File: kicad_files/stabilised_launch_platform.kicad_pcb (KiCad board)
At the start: 2 copper layers, 77 x 64.6 mm, 37 parts, among them J1 Conn_01x03_Male, J2 Conn_01x03_Male, J3 Conn_01x06_Male, J4 USB_C_Receptacle_USB2.0, SW1 SW_Push, U1 MAX7375AXR805, U2 AP7370-33Y, U3 STM32L011F3Px, U4 FT201XS, U5 LIS3DH

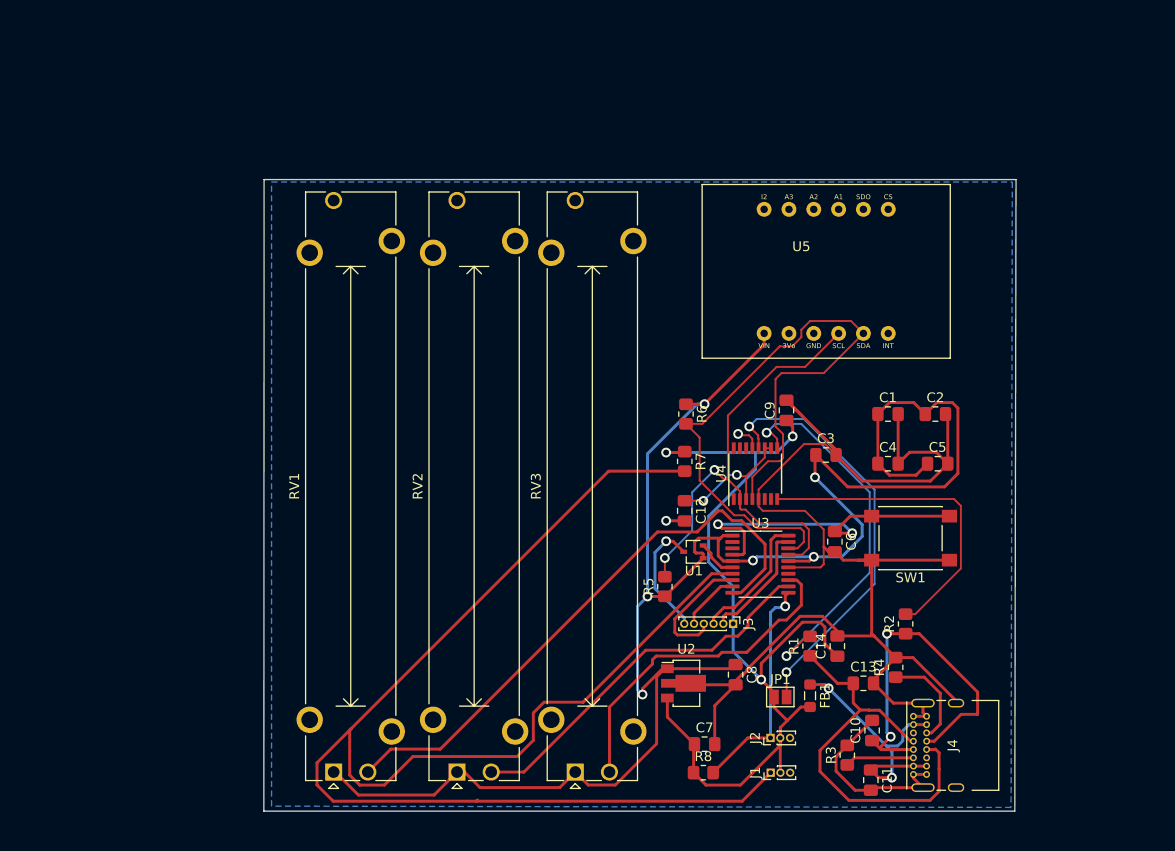
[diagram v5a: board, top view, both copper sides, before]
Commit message: PCB modifications: R1 and R2 moved closer to ftdi chip, 3.5mm diameter screw holes added, rounded PCB corners, C14 now electrolyic capacitor
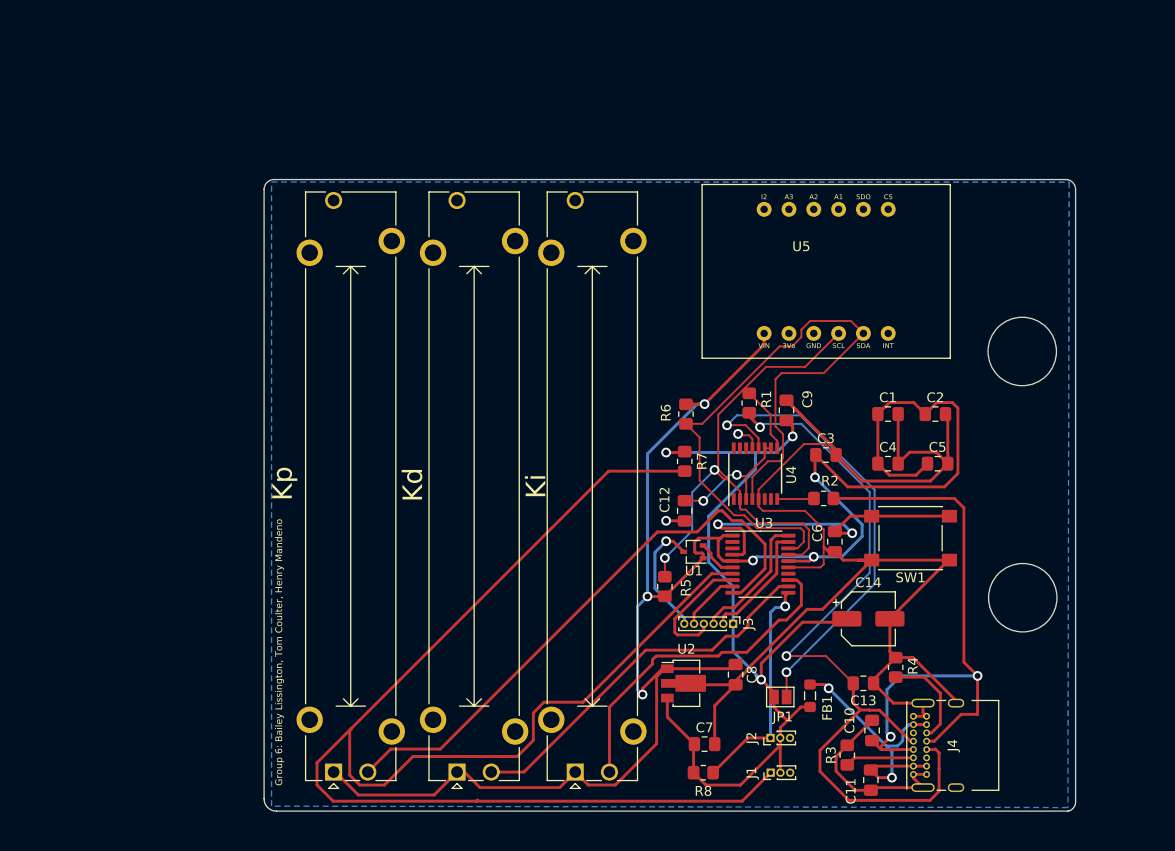
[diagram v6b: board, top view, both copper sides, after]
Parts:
- C14: footprint Capacitor_SMD:C_0805_2012Metric_Pad1.18x1.45mm_HandSolder -> Capacitor_SMD:CP_Elec_5x3
- moved R1 25.6 mm to (136.3, 84.0)
- moved R2 15.3 mm to (143.9, 93.7), turned to 180 degrees
- moved C14 4.23 mm to (148.5, 106.0), turned to 0 degrees
- renumbered RV2 to Kd, RV3 to Ki, RV1 to Kp
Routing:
- net USBDM: track 42.6 -> 81.4 mm, vias 0 -> 2
- net Net-(R1-Pad2): track 39.7 -> 6.81 mm, vias 2 -> 0
- net Net-(R2-Pad2): track 33.1 -> 3.79 mm
- net USBDP: track 37.4 -> 63.0 mm
- net Net-(JP1-Pad2): track 43.7 -> 48.4 mm
- net GND: track 182.1 -> 184.9 mm
- net SCL: track 51.9 -> 53.3 mm
- net +5V: track 93.8 -> 92.5 mm
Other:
- board size 77 x 64.6 mm -> 83.1 x 64.6 mm
- board text added: "Group 6: Bailey Lissington, Tom Coulter, Henry Mandeno"
